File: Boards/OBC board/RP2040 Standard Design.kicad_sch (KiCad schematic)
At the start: 38 parts, among them J1 BM03B-SRSS-TBLFSN, J2 DX07S016JA1R1500, U1 W25Q128JVSIQ TR, U11 ST1L05APU33R, U2 ESD7L5.0DT5G

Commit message: Mudança de nome das footprints
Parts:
- CV1, CV10, CV11, CV12, CV13, CV14, CV17, CV18, CV2, CV3, CV4, CV5, CV6, CV7, CV8, CV9: footprint CAP_GCM155_MUR:CAP_GCM155_MUR -> Capacitor_0402:Capacitor_0402
- CV15, CV16: footprint GRM15x:GRM15x -> C_4uF7_0402:C_4uF7_0402
- R1, R4, R5, R6, R7, R8: footprint RC0402N_VIS:RC0402N_VIS -> RES_0402:RES_0402
- R2, R3: footprint KTR03EZPF27R0:RES_R0603_ROM -> RES_R0603_27:RES_R0603_27
- R9: footprint RC0402N_VIS:RC0402N_VIS -> R_0805_5K1:R_0805_5K1
- RC1: footprint ERA6AEB101V:ERA6AEB101V -> R_0805_5K1:R_0805_5K1
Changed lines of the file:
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@@
 			)
 		)
-		(property "Footprint" "RC0402N_VIS:RC0402N_VIS"
+		(property "Footprint" "RES_0402:RES_0402"
 			(at 18.542 65.405 90)
 			(effects
@@
 			)
 		)
-		(property "Footprint" "CAP_GCM155_MUR:CAP_GCM155_MUR"
+		(property "Footprint" "Capacitor_0402:Capacitor_0402"
 			(at 64.4652 62.23 0)
 			(effects
@@
 			)
 		)
-		(property "Footprint" "CAP_GCM155_MUR:CAP_GCM155_MUR"
+		(property "Footprint" "Capacitor_0402:Capacitor_0402"
 			(at 122.2502 50.165 0)
 			(effects
@@
 			)
 		)
-		(property "Footprint" "CAP_GCM155_MUR:CAP_GCM155_MUR"
+		(property "Footprint" "Capacitor_0402:Capacitor_0402"
 			(at 132.08 177.4698 0)
 			(effects
@@
 			)
 		)
-		(property "Footprint" "CAP_GCM155_MUR:CAP_GCM155_MUR"
+		(property "Footprint" "Capacitor_0402:Capacitor_0402"
 			(at 129.2352 50.165 0)
 			(effects
@@
 			)
 		)
-		(property "Footprint" "RC0402N_VIS:RC0402N_VIS"
+		(property "Footprint" "RES_0402:RES_0402"
 			(at 41.91 138.557 90)
 			(effects
@@
 			)
 		)
-		(property "Footprint" "ERA6AEB101V:ERA6AEB101V"
+		(property "Footprint" "R_0805_5K1:R_0805_5K1"
 			(at 181.102 139.7 90)
 			(effects
@@
 			)
 		)
-		(property "Footprint" "CAP_GCM155_MUR:CAP_GCM155_MUR"
+		(property "Footprint" "Capacitor_0402:Capacitor_0402"
 			(at 190.1698 89.535 0)
 			(effects
@@
 			)
 		)
-		(property "Footprint" "CAP_GCM155_MUR:CAP_GCM155_MUR"
+		(property "Footprint" "Capacitor_0402:Capacitor_0402"
 			(at 87.3252 59.69 0)
 			(effects
@@
 			)
 		)
-		(property "Footprint" "CAP_GCM155_MUR:CAP_GCM155_MUR"
+		(property "Footprint" "Capacitor_0402:Capacitor_0402"
 			(at 136.2202 50.165 0)
 			(effects
@@
 			)
 		)
-		(property "Footprint" "RC0402N_VIS:RC0402N_VIS"
+		(property "Footprint" "RES_0402:RES_0402"
 			(at 177.927 40.005 90)
 			(effects
@@
 			)
 		)
-		(property "Footprint" "CAP_GCM155_MUR:CAP_GCM155_MUR"
+		(property "Footprint" "Capacitor_0402:Capacitor_0402"
 			(at 32.6898 61.595 0)
 			(effects
@@
 			)
 		)
-		(property "Footprint" "CAP_GCM155_MUR:CAP_GCM155_MUR"
+		(property "Footprint" "Capacitor_0402:Capacitor_0402"
 			(at 101.2952 50.165 0)
 			(effects
@@
 			)
 		)
-		(property "Footprint" "CAP_GCM155_MUR:CAP_GCM155_MUR"
+		(property "Footprint" "Capacitor_0402:Capacitor_0402"
 			(at 272.7452 41.91 0)
 			(effects
@@
 			)
 		)
-		(property "Footprint" "CAP_GCM155_MUR:CAP_GCM155_MUR"
+		(property "Footprint" "Capacitor_0402:Capacitor_0402"
 			(at 94.3102 50.165 0)
 			(effects
@@
 			)
 		)
-		(property "Footprint" "RC0402N_VIS:RC0402N_VIS"
+		(property "Footprint" "RES_0402:RES_0402"
 			(at 55.372 177.8 90)
 			(effects
@@
 			)
 		)
-		(property "Footprint" "RC0402N_VIS:RC0402N_VIS"
+		(property "Footprint" "R_0805_5K1:R_0805_5K1"
 			(at 175.387 137.795 90)
 			(effects
@@
 			)
 		)
-		(property "Footprint" "CAP_GCM155_MUR:CAP_GCM155_MUR"
+		(property "Footprint" "Capacitor_0402:Capacitor_0402"
 			(at 115.2652 50.165 0)
 			(effects
@@
 			)
 		)
-		(property "Footprint" "GRM15x:GRM15x"
+		(property "Footprint" "C_4uF7_0402:C_4uF7_0402"
 			(at 190.1698 85.725 0)
 			(effects
@@
 			)
 		)
-		(property "Footprint" "KTR03EZPF27R0:RES_R0603_ROM"
+		(property "Footprint" "RES_R0603_27:RES_R0603_27"
 			(at 41.275 79.883 90)
 			(effects
@@
 			)
 		)
-		(property "Footprint" "CAP_GCM155_MUR:CAP_GCM155_MUR"
+		(property "Footprint" "Capacitor_0402:Capacitor_0402"
 			(at 108.2802 50.165 0)
 			(effects
@@
 			)
 		)
-		(property "Footprint" "CAP_GCM155_MUR:CAP_GCM155_MUR"
+		(property "Footprint" "Capacitor_0402:Capacitor_0402"
 			(at 87.3252 50.165 0)
 			(effects
@@
 			)
 		)
-		(property "Footprint" "CAP_GCM155_MUR:CAP_GCM155_MUR"
+		(property "Footprint" "Capacitor_0402:Capacitor_0402"
 			(at 56.8198 42.545 0)
 			(effects
@@
 			)
 		)
-		(property "Footprint" "CAP_GCM155_MUR:CAP_GCM155_MUR"
+		(property "Footprint" "Capacitor_0402:Capacitor_0402"
 			(at 64.4398 42.545 0)
 			(effects
@@
 			)
 		)
-		(property "Footprint" "RC0402N_VIS:RC0402N_VIS"
+		(property "Footprint" "RES_0402:RES_0402"
 			(at 41.91 133.477 90)
 			(effects
@@
 			)
 		)
-		(property "Footprint" "KTR03EZPF27R0:RES_R0603_ROM"
+		(property "Footprint" "RES_R0603_27:RES_R0603_27"
 			(at 41.275 78.867 90)
 			(effects
@@
 			)
 		)
-		(property "Footprint" "GRM15x:GRM15x"
+		(property "Footprint" "C_4uF7_0402:C_4uF7_0402"
 			(at 177.4698 90.17 0)
 			(effects
@@
 			)
 		)
-		(property "Footprint" "RC0402N_VIS:RC0402N_VIS"
+		(property "Footprint" "RES_0402:RES_0402"
 			(at 43.942 64.77 90)
 			(effects

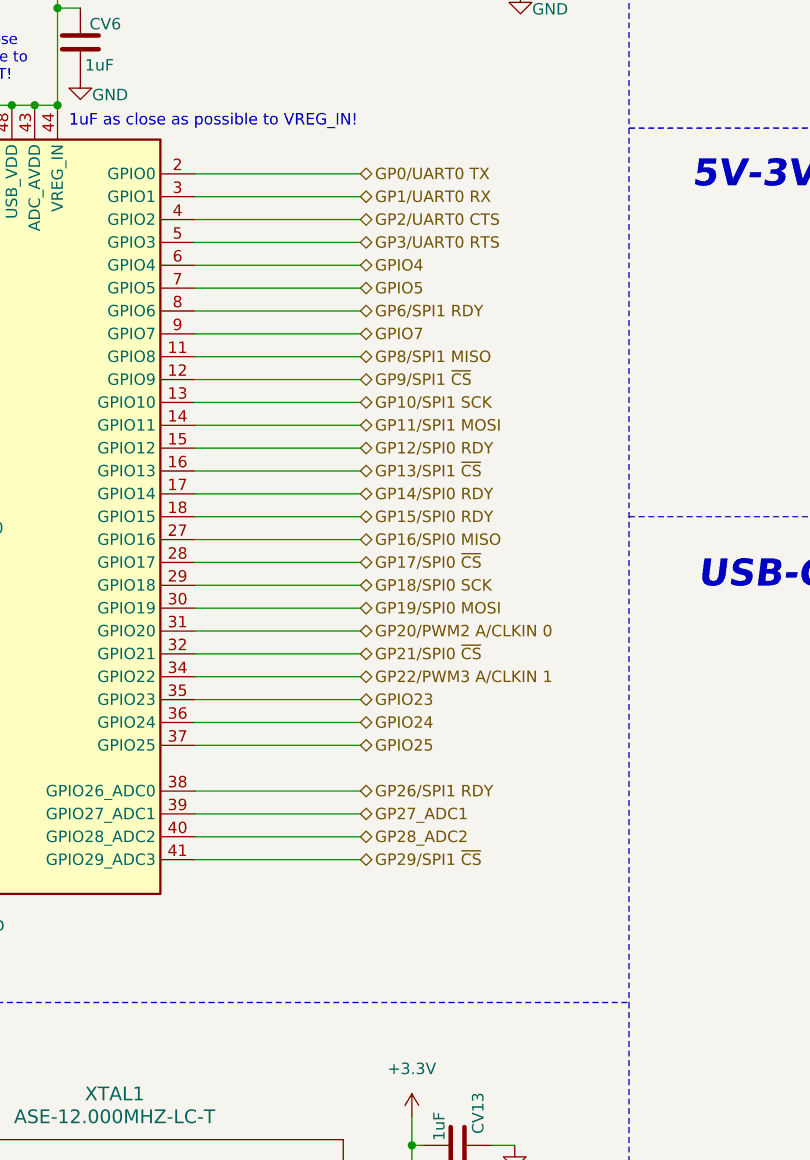
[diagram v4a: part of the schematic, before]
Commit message: changes in RP2040 design
GPIO25 LED is now part of RP2040 Standard
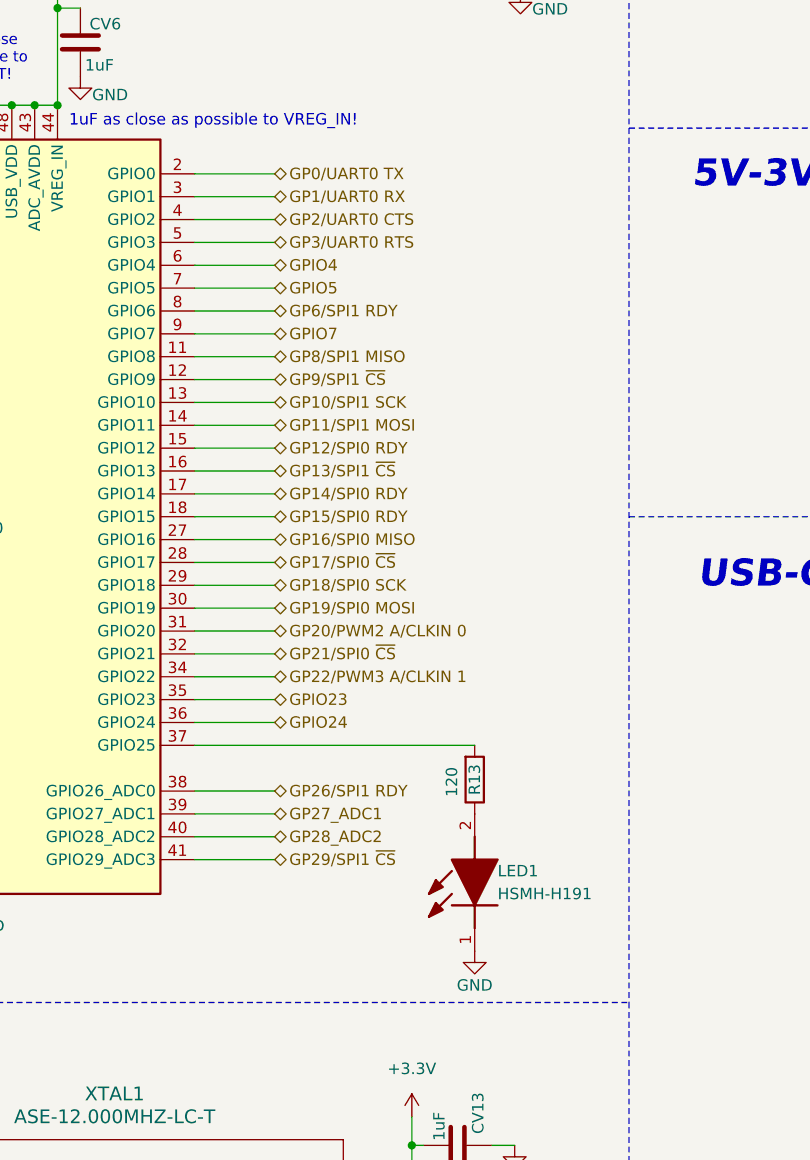
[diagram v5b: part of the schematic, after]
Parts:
- added LED1: HSMH-H191, MAG LIS2MDLTR:LGA-12_2X2X1_STM, symbol Red SMD LED:HSMH-H191
- added R13: 120, RC0402N_VIS:RC0402N_VIS, symbol Device:R
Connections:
- net GND: now also LED1.1 (K)
- net GPIO25: no longer names the net of MCU1.37 (GPIO25)
- net GPIO25: now also R13.2
- new net: LED1.2 (A), R13.1
